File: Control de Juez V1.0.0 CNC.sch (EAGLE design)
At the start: 31 parts, among them IC1 MEGA48/88/168-AU, Q1 MMBT3904, Q2 MMBT3904, Q3 MMBT3904, SW1 JS202011CQN, SW2 3-1825910-1, SW3 3-1825910-1, SW4 3-1825910-1

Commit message: Add files via upload
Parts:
- removed C2, C3: 0.1uF, rcl:C-EUC0603
- removed IC1: MEGA48/88/168-AU, avr-8:MEGA48/88/168-AU
- removed JP1, JP3: (no value), pinhead-2:PINHD-1X02_2.54-S
- removed JP2: (no value), pinhead-2:PINHD-1X04_2.54-S
- removed L1: 10uH, rcl:L-USL1812
- removed LED4: (no value), led:LEDCHIP-LED0603
- removed Q2, Q3: MMBT3904, FAIRCHILD-MMBT3904_Transistor:MMBT3904
- removed R3, R4: 1K, rcl:R-US_R0603
- removed R5: 330E, rcl:R-US_R0603
- removed R7, R8, R9: 10K, rcl:R-US_R0603
- removed SW1: JS202011CQN, C&K-Slider_Switch:JS202011CQN
- removed SW2, SW3, SW4: 3-1825910-1, TE-Push_button:3-1825910-1
- added BT2: BU2032SM-HD-G, BU2032SM-HD-G:BU2032SM-HD-G
- added GND, UPDI, V+: TPB1,27, testpad:TPB1,27
- added GO, READY, RESET: EVQ-P7L01P, EVQ-P7L01P:EVQ-P7L01P
- added GOLD_ORB_SM1: OSHWLOGOLOGO8MM, oshw:OSHWLOGOLOGO8MM
- added S1: JS102011SAQN, JS102011SAQN:JS102011SAQN
- added U1: ATTINY412-SSNSOIC8_SA_SST_MCH-M, attiny412:ATTINY412-SSNSOIC8_SA_SST_MCH-M
- BT1: value HOLD-BATTERY-3-AAA -> BU2032SM-HD-G; device BATTERY_HOLDER_3AAA-C9091:HOLD-BATTERY-3-AAA -> BU2032SM-HD-G:BU2032SM-HD-G
- LED5: device led:LEDCHIP-LED0603 -> led:LEDSML1206
- R1: value 10K -> 1K
- R6: value 330E -> 1k
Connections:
- removed net N$10: Q3.B, R4.1
- removed net N$11: Q2.B, R3.1
- removed net N$13: LED5.C, R5.1
- removed net N$15: LED4.A, R5.2
- removed net N$5: IC1.PB5(SCK/PCINT5), JP2.2
- removed net N$6: JP3.1, SW1.1.1, SW1.1.2, SW1.2.1, SW1.2.2
- removed net N$7: LED1.C, Q1.C
- removed net N$8: LED2.C, Q2.C
- removed net N$9: LED3.C, Q3.C
- removed net RESET: IC1.PC6(/RESET/PCINT14), JP2.3, R1.1
- net +5V: now also BT1.+, BT2.+, U1.VDD, V+.TP; no longer IC1.VCC@1, IC1.VCC@2, JP1.1, L1.2, R1.2, R7.2, R8.2, R9.2, SW1.3.1, SW1.3.2
- net GND: now also GND.TP, GO.1, READY.1, RESET.1, S1.3, U1.GND; no longer C2.2, C3.2, IC1.AGND, IC1.GND@1, IC1.GND@2, JP1.2, JP3.2, Q2.E, Q3.E, SW2.1, SW2.2, SW3.1, SW3.2, SW4.1, SW4.2
- net GO: now also GO.2, U1.PA7; no longer IC1.PD1(TXD/PCINT17), R9.1, SW4.3, SW4.4
- net LEDS: now also U1.PA2; no longer IC1.PB1(OC1A/PCINT1), R3.2, R4.2
- net LEDSMD: now also LED5.C, U1.PA1; no longer IC1.PD2(INT0/PCINT18), LED4.C
- net N$1: now also U1.PA0/!RESET/UPDI, UPDI.TP; no longer IC1.PB3(MOSI/OC2A/PCINT3), JP2.4
- net N$2: now also BT1.-, BT2.-, S1.1, S1.2; no longer C3.1, IC1.AVCC, L1.1
- net N$3: now also LED1.C, LED2.C, LED3.C, R1.1; no longer C2.1, IC1.AREF
- net N$4: now also Q1.C, R1.2; no longer IC1.PB4(MISO/PCINT4), JP2.1
- net READY: now also READY.2, U1.PA6; no longer IC1.PD3(INT1/OC2B/PCINT19), R7.1, SW2.3, SW2.4
- net RST: now also RESET.2, U1.PA3/EXTCLK; no longer IC1.PD0(RXD/PCINT16), R8.1, SW3.3, SW3.4
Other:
- note added: "Capacitores de bypass y bulk, de acondicionamiento de potencia"
- note removed: "Base Baterias"
- note removed: "Capacitor de almacenamiento de energia para Baterias"
- moved on the sheet: C1, LED1, LED2, LED3, R1

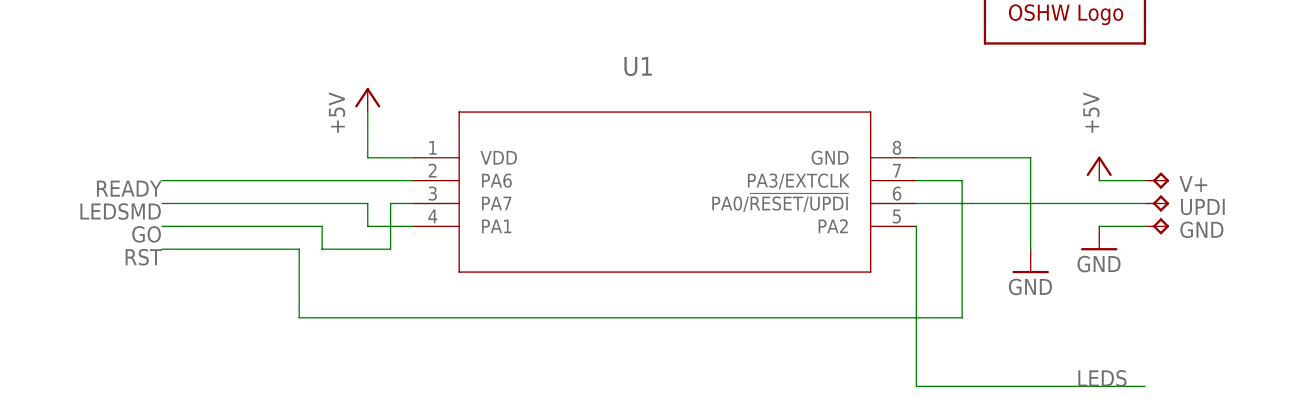
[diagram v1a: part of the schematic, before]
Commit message: Add files via upload
Reconexiones para mejor programación ocupando el hardware del microcontrolador
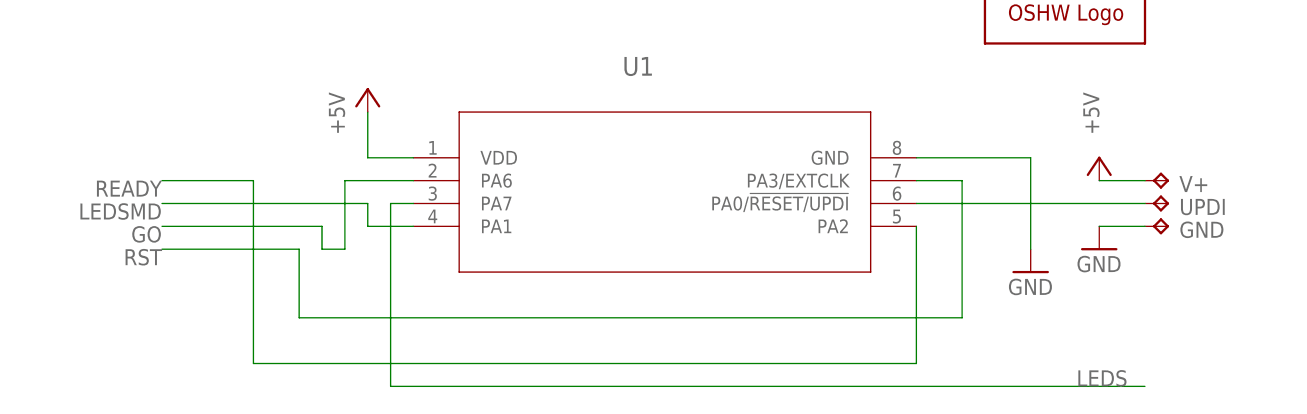
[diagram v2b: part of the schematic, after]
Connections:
- net GO: now also U1.PA6; no longer U1.PA7
- net LEDS: now also U1.PA7; no longer U1.PA2
- net READY: now also U1.PA2; no longer U1.PA6
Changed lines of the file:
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@@
 </segment>
 <segment>
-<wire x1="73.66" y1="20.32" x2="99.06" y2="20.32" width="0.1524" layer="91"/>
 <label x="91.44" y="20.32" size="1.778" layer="95"/>
-<pinref part="U1" gate="A" pin="PA2"/>
-<wire x1="73.66" y1="38.1" x2="73.66" y2="20.32" width="0.1524" layer="91"/>
+<wire x1="99.06" y1="20.32" x2="15.24" y2="20.32" width="0.1524" layer="91"/>
+<wire x1="15.24" y1="20.32" x2="15.24" y2="40.64" width="0.1524" layer="91"/>
+<pinref part="U1" gate="A" pin="PA7"/>
+<wire x1="15.24" y1="40.64" x2="17.78" y2="40.64" width="0.1524" layer="91"/>
 </segment>
 </net>
@@
 <wire x1="12.7" y1="40.64" x2="-10.16" y2="40.64" width="0.1524" layer="91"/>
 <pinref part="U1" gate="A" pin="PA1"/>
-<wire x1="17.78" y1="38.1" x2="12.7" y2="38.1" width="0.1524" layer="91"/>
-<wire x1="12.7" y1="38.1" x2="12.7" y2="40.64" width="0.1524" layer="91"/>
+<wire x1="12.7" y1="40.64" x2="12.7" y2="38.1" width="0.1524" layer="91"/>
+<wire x1="12.7" y1="38.1" x2="17.78" y2="38.1" width="0.1524" layer="91"/>
 </segment>
 <segment>
@@
 <label x="-10.16" y="38.1" size="1.778" layer="95" rot="R180"/>
 <wire x1="7.62" y1="38.1" x2="-10.16" y2="38.1" width="0.1524" layer="91"/>
-<pinref part="U1" gate="A" pin="PA7"/>
-<wire x1="17.78" y1="40.64" x2="15.24" y2="40.64" width="0.1524" layer="91"/>
-<wire x1="15.24" y1="40.64" x2="15.24" y2="35.56" width="0.1524" layer="91"/>
-<wire x1="15.24" y1="35.56" x2="7.62" y2="35.56" width="0.1524" layer="91"/>
 <wire x1="7.62" y1="35.56" x2="7.62" y2="38.1" width="0.1524" layer="91"/>
+<wire x1="7.62" y1="35.56" x2="10.16" y2="35.56" width="0.1524" layer="91"/>
+<pinref part="U1" gate="A" pin="PA6"/>
+<wire x1="10.16" y1="35.56" x2="10.16" y2="43.18" width="0.1524" layer="91"/>
+<wire x1="10.16" y1="43.18" x2="17.78" y2="43.18" width="0.1524" layer="91"/>
 </segment>
 <segment>
@@
 <net name="READY" class="0">
 <segment>
-<wire x1="17.78" y1="43.18" x2="-10.16" y2="43.18" width="0.1524" layer="91"/>
 <label x="-10.16" y="43.18" size="1.778" layer="95" rot="R180"/>
-<pinref part="U1" gate="A" pin="PA6"/>
+<wire x1="0" y1="43.18" x2="-10.16" y2="43.18" width="0.1524" layer="91"/>
+<wire x1="0" y1="43.18" x2="0" y2="22.86" width="0.1524" layer="91"/>
+<wire x1="0" y1="22.86" x2="73.66" y2="22.86" width="0.1524" layer="91"/>
+<pinref part="U1" gate="A" pin="PA2"/>
+<wire x1="73.66" y1="22.86" x2="73.66" y2="38.1" width="0.1524" layer="91"/>
 </segment>
 <segment>

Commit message: Add files via upload
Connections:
- net LEDSMD renamed LEDSTATUS
- removed net LEDS: R2.2, U1.PA7
- removed net RST: RESET.2, U1.PA3/EXTCLK
- new net LEDTRANSMISION: R2.2, U1.PA2
- new net RESET: READY.2, U1.PA6
- net GO: now also U1.PA7; no longer U1.PA6
- net READY: now also RESET.2, U1.PA3/EXTCLK; no longer READY.2, U1.PA2
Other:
- moved on the sheet: BT1, BT2, C1, C4, GO, LED1, LED2, LED3, LED5, Q1, R1, R2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

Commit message: Add files via upload
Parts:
- removed U1: ATTINY412-SSNSOIC8_SA_SST_MCH-M, attiny412:ATTINY412-SSNSOIC8_SA_SST_MCH-M
- added U2: ATTINY1614-SSNR, Attiny1614:ATTINY1614-SSNR
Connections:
- removed net N$1: U1.PA0/!RESET/UPDI, UPDI.TP
- new net UPDI: U2.PA0/!RESET/UPDI, UPDI.TP
- net +5V: now also U2.VDD; no longer U1.VDD
- net GND: now also U2.GND; no longer U1.GND
- net GO: now also U2.PA7; no longer U1.PA7
- net LEDSTATUS: now also U2./PB3; no longer U1.PA1
- net LEDTRANSMISION: now also U2.PA4; no longer U1.PA2
- net READY: now also U2.PA6; no longer U1.PA3/EXTCLK
- net RESET: now also U2./PB2; no longer U1.PA6
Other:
- moved on the sheet: UPDI
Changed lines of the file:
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@@
 <part name="GND12" library="supply1" library_urn="urn:adsk.eagle:library:371" deviceset="GND" device=""/>
 <part name="GND13" library="supply1" library_urn="urn:adsk.eagle:library:371" deviceset="GND" device=""/>
-<part name="U1" library="attiny412" deviceset="ATTINY412-SSN" device="SOIC8_SA_SST_MCH-M"/>
 <part name="S1" library="JS102011SAQN" deviceset="JS102011SAQN" device=""/>
 <part name="P+1" library="supply1" library_urn="urn:adsk.eagle:library:371" deviceset="+5V" device=""/>
@@
 <part name="BT1" library="BU2032SM-HD-G" deviceset="BU2032SM-HD-G" device=""/>
 <part name="GOLD_ORB_SM1" library="oshw" deviceset="OSHWLOGO" device="LOGO8MM"/>
+<part name="U2" library="Attiny1614" deviceset="ATTINY1614-SSNR" device=""/>
 </parts>
 <sheets>
@@
 </plain>
 <instances>
-<instance part="GND1" gate="1" x="86.36" y="33.02" smashed="yes">
-<attribute name="VALUE" x="83.82" y="30.48" size="1.778" layer="96"/>
+<instance part="GND1" gate="1" x="2.54" y="22.86" smashed="yes">
+<attribute name="VALUE" x="0" y="20.32" size="1.778" layer="96"/>
 </instance>
 <instance part="C1" gate="G$1" x="-33.02" y="91.44" smashed="yes">
@@
 <attribute name="VALUE" x="93.98" y="71.12" size="1.778" layer="96"/>
 </instance>
-<instance part="U1" gate="A" x="15.24" y="45.72" smashed="yes">
-<attribute name="NAME" x="40.9956" y="54.8386" size="2.0828" layer="95" ratio="6" rot="SR0"/>
-</instance>
 <instance part="S1" gate="G$1" x="-50.8" y="22.86" smashed="yes">
 <attribute name="NAME" x="-58.422909375" y="27.941940625" size="1.270490625" layer="95"/>
 <attribute name="VALUE" x="-58.428559375" y="17.774290625" size="1.27143125" layer="96"/>
 </instance>
-<instance part="P+1" gate="1" x="12.7" y="53.34" smashed="yes">
-<attribute name="VALUE" x="10.16" y="48.26" size="1.778" layer="96" rot="R90"/>
+<instance part="P+1" gate="1" x="66.04" y="53.34" smashed="yes">
+<attribute name="VALUE" x="63.5" y="48.26" size="1.778" layer="96" rot="R90"/>
 </instance>
 <instance part="V+" gate="G$1" x="101.6" y="43.18" smashed="yes" rot="R270">
@@
 <attribute name="TP_SIGNAL_NAME" x="100.33" y="41.91" size="1.778" layer="97" rot="R270"/>
 </instance>
-<instance part="UPDI" gate="G$1" x="101.6" y="40.64" smashed="yes" rot="R270">
-<attribute name="NAME" x="102.87" y="39.37" size="1.778" layer="95"/>
-<attribute name="TP_SIGNAL_NAME" x="100.33" y="39.37" size="1.778" layer="97" rot="R270"/>
+<instance part="UPDI" gate="G$1" x="0" y="55.88" smashed="yes">
+<attribute name="NAME" x="1.27" y="57.15" size="1.778" layer="95" rot="R90"/>
+<attribute name="TP_SIGNAL_NAME" x="1.27" y="54.61" size="1.778" layer="97"/>
 </instance>
 <instance part="GND" gate="G$1" x="101.6" y="38.1" smashed="yes" rot="R270">
@@
 </instance>
 <instance part="GOLD_ORB_SM1" gate="G$1" x="81.28" y="58.42" smashed="yes"/>
+<instance part="U2" gate="A" x="66.04" y="30.48" smashed="yes" rot="R180">
+<attribute name="NAME" x="37.7444" y="21.3614" size="2.0828" layer="95" ratio="6" rot="SR180"/>
+<attribute name="VALUE" x="38.3794" y="23.9014" size="2.0828" layer="96" ratio="6" rot="SR180"/>
+</instance>
 </instances>
 <busses>
@@
 <pinref part="R6" gate="G$1" pin="1"/>
 <wire x1="76.2" y1="160.02" x2="76.2" y2="154.94" width="0.1524" layer="91"/>
-</segment>
-<segment>
-<pinref part="P+1" gate="1" pin="+5V"/>
-<pinref part="U1" gate="A" pin="VDD"/>
-<wire x1="12.7" y1="50.8" x2="12.7" y2="45.72" width="0.1524" layer="91"/>
-<wire x1="12.7" y1="45.72" x2="17.78" y2="45.72" width="0.1524" layer="91"/>
 </segment>
 <segment>
@@
 <junction x="-60.96" y="40.64"/>
 </segment>
+<segment>
+<pinref part="U2" gate="A" pin="VDD"/>
+<pinref part="P+1" gate="1" pin="+5V"/>
+<wire x1="63.5" y1="30.48" x2="66.04" y2="30.48" width="0.1524" layer="91"/>
+<wire x1="66.04" y1="30.48" x2="66.04" y2="50.8" width="0.1524" layer="91"/>
+</segment>
 </net>
 <net name="GND" class="0">
@@
 </segment>
 <segment>
-<pinref part="U1" gate="A" pin="GND"/>
-<pinref part="GND1" gate="1" pin="GND"/>
-<wire x1="73.66" y1="45.72" x2="86.36" y2="45.72" width="0.1524" layer="91"/>
-<wire x1="86.36" y1="45.72" x2="86.36" y2="35.56" width="0.1524" layer="91"/>
-</segment>
-<segment>
 <wire x1="93.98" y1="38.1" x2="99.06" y2="38.1" width="0.1524" layer="91"/>
 <pinref part="GND" gate="G$1" pin="TP"/>
@@
 <wire x1="-60.96" y1="20.32" x2="-60.96" y2="17.78" width="0.1524" layer="91"/>
 </segment>
+<segment>
+<pinref part="U2" gate="A" pin="GND"/>
+<pinref part="GND1" gate="1" pin="GND"/>
+<wire x1="2.54" y1="30.48" x2="2.54" y2="25.4" width="0.1524" layer="91"/>
+</segment>
 </net>
 <net name="N$12" class="0">
@@
 <wire x1="73.66" y1="20.32" x2="99.06" y2="20.32" width="0.1524" layer="91"/>
 <label x="91.44" y="20.32" size="1.778" layer="95"/>
-<pinref part="U1" gate="A" pin="PA2"/>
-<wire x1="73.66" y1="38.1" x2="73.66" y2="20.32" width="0.1524" layer="91"/>
+<pinref part="U2" gate="A" pin="PA4"/>
+<wire x1="73.66" y1="33.02" x2="73.66" y2="20.32" width="0.1524" layer="91"/>
+<wire x1="63.5" y1="33.02" x2="73.66" y2="33.02" width="0.1524" layer="91"/>
 </segment>
 </net>
@@
 <net name="LEDSTATUS" class="0">
 <segment>
-<label x="-10.16" y="40.64" size="1.778" layer="95" rot="R180"/>
-<wire x1="12.7" y1="40.64" x2="-10.16" y2="40.64" width="0.1524" layer="91"/>
-<pinref part="U1" gate="A" pin="PA1"/>
-<wire x1="17.78" y1="38.1" x2="12.7" y2="38.1" width="0.1524" layer="91"/>
-<wire x1="12.7" y1="38.1" x2="12.7" y2="40.64" width="0.1524" layer="91"/>
+<label x="-33.02" y="40.64" size="1.778" layer="95" rot="R180"/>
+<wire x1="-2.54" y1="40.64" x2="-33.02" y2="40.64" width="0.1524" layer="91"/>
+<wire x1="-2.54" y1="40.64" x2="-2.54" y2="58.42" width="0.1524" layer="91"/>
+<wire x1="-2.54" y1="58.42" x2="68.58" y2="58.42" width="0.1524" layer="91"/>
+<pinref part="U2" gate="A" pin="/PB3"/>
+<wire x1="68.58" y1="58.42" x2="68.58" y2="43.18" width="0.1524" layer="91"/>
+<wire x1="68.58" y1="43.18" x2="63.5" y2="43.18" width="0.1524" layer="91"/>
 </segment>
 <segment>
@@
 <net name="READY" class="0">
 <segment>
-<wire x1="5.08" y1="35.56" x2="-10.16" y2="35.56" width="0.1524" layer="91"/>
-<label x="-10.16" y="35.56" size="1.778" layer="95" rot="R180"/>
-<wire x1="5.08" y1="35.56" x2="5.08" y2="27.94" width="0.1524" layer="91"/>
-<wire x1="5.08" y1="27.94" x2="78.74" y2="27.94" width="0.1524" layer="91"/>
-<pinref part="U1" gate="A" pin="PA3/EXTCLK"/>
-<wire x1="78.74" y1="27.94" x2="78.74" y2="43.18" width="0.1524" layer="91"/>
-<wire x1="78.74" y1="43.18" x2="73.66" y2="43.18" width="0.1524" layer="91"/>
+<wire x1="-17.78" y1="35.56" x2="-33.02" y2="35.56" width="0.1524" layer="91"/>
+<label x="-33.02" y="35.56" size="1.778" layer="95" rot="R180"/>
+<wire x1="-17.78" y1="35.56" x2="-17.78" y2="27.94" width="0.1524" layer="91"/>
+<wire x1="-17.78" y1="27.94" x2="78.74" y2="27.94" width="0.1524" layer="91"/>
+<wire x1="78.74" y1="27.94" x2="78.74" y2="38.1" width="0.1524" layer="91"/>
+<pinref part="U2" gate="A" pin="PA6"/>
+<wire x1="63.5" y1="38.1" x2="78.74" y2="38.1" width="0.1524" layer="91"/>
 </segment>
 <segment>
@@
 <net name="GO" class="0">
 <segment>
-<label x="-10.16" y="38.1" size="1.778" layer="95" rot="R180"/>
-<wire x1="7.62" y1="38.1" x2="-10.16" y2="38.1" width="0.1524" layer="91"/>
-<pinref part="U1" gate="A" pin="PA7"/>
-<wire x1="17.78" y1="40.64" x2="15.24" y2="40.64" width="0.1524" layer="91"/>
-<wire x1="15.24" y1="40.64" x2="15.24" y2="35.56" width="0.1524" layer="91"/>
-<wire x1="15.24" y1="35.56" x2="7.62" y2="35.56" width="0.1524" layer="91"/>
-<wire x1="7.62" y1="35.56" x2="7.62" y2="38.1" width="0.1524" layer="91"/>
+<label x="-33.02" y="38.1" size="1.778" layer="95" rot="R180"/>
+<wire x1="-7.62" y1="38.1" x2="-33.02" y2="38.1" width="0.1524" layer="91"/>
+<wire x1="-7.62" y1="38.1" x2="-7.62" y2="71.12" width="0.1524" layer="91"/>
+<wire x1="-7.62" y1="71.12" x2="71.12" y2="71.12" width="0.1524" layer="91"/>
+<wire x1="71.12" y1="71.12" x2="71.12" y2="40.64" width="0.1524" layer="91"/>
+<pinref part="U2" gate="A" pin="PA7"/>
+<wire x1="71.12" y1="40.64" x2="63.5" y2="40.64" width="0.1524" layer="91"/>
 </segment>
 <segment>
@@
 <net name="RESET" class="0">
 <segment>
-<wire x1="17.78" y1="43.18" x2="-10.16" y2="43.18" width="0.1524" layer="91"/>
-<label x="-10.16" y="43.18" size="1.778" layer="95" rot="R180"/>
-<pinref part="U1" gate="A" pin="PA6"/>
+<wire x1="-15.24" y1="43.18" x2="-33.02" y2="43.18" width="0.1524" layer="91"/>
+<label x="-33.02" y="43.18" size="1.778" layer="95" rot="R180"/>
+<wire x1="-15.24" y1="43.18" x2="-15.24" y2="63.5" width="0.1524" layer="91"/>
+<pinref part="U2" gate="A" pin="/PB2"/>
+<wire x1="-15.24" y1="63.5" x2="63.5" y2="63.5" width="0.1524" layer="91"/>
+<wire x1="63.5" y1="63.5" x2="63.5" y2="45.72" width="0.1524" layer="91"/>
 </segment>
 <segment>
@@
 <pinref part="READY" gate="G$1" pin="2"/>
 <wire x1="2.54" y1="96.52" x2="2.54" y2="83.82" width="0.1524" layer="91"/>
-</segment>
-</net>
-<net name="N$1" class="0">
-<segment>
-<pinref part="U1" gate="A" pin="PA0/!RESET/UPDI"/>
-<wire x1="73.66" y1="40.64" x2="99.06" y2="40.64" width="0.1524" layer="91"/>
-<pinref part="UPDI" gate="G$1" pin="TP"/>
 </segment>
 </net>
@@
 </segment>
 </net>
+<net name="UPDI" class="0">
+<segment>
+<pinref part="U2" gate="A" pin="PA0/!RESET/UPDI"/>
+<pinref part="UPDI" gate="G$1" pin="TP"/>
+<wire x1="2.54" y1="40.64" x2="0" y2="40.64" width="0.1524" layer="91"/>
+<wire x1="0" y1="40.64" x2="0" y2="53.34" width="0.1524" layer="91"/>
+</segment>
+</net>
